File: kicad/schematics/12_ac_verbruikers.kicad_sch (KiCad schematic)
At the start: 6 parts

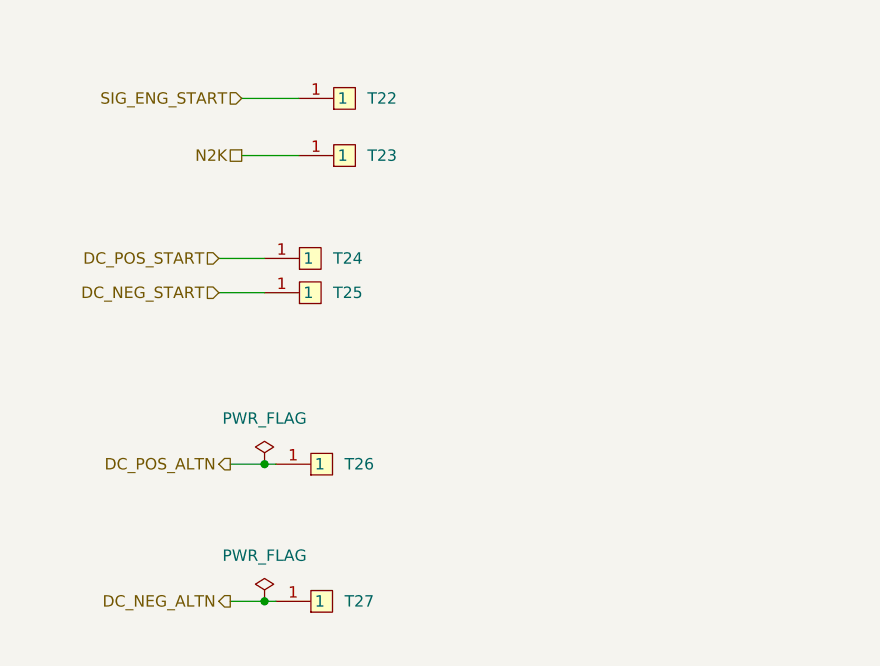
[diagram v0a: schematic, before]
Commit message: Introductie schema 15_energieconversie
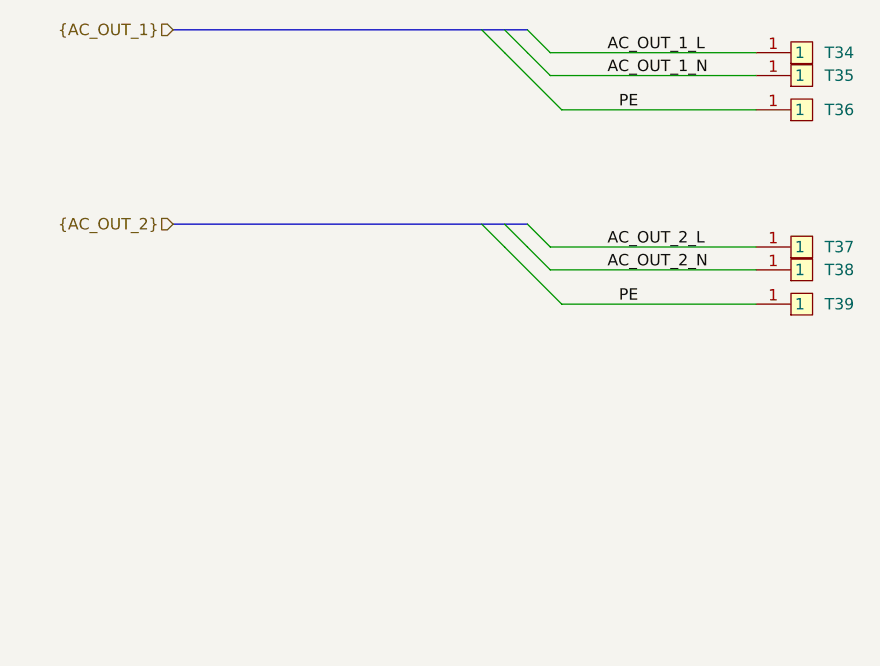
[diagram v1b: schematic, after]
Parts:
- removed T22, T23: (no value), symbol falkor-electrical:IF_Passief
- removed T24, T25, T26, T27: (no value), symbol falkor-electrical:IF_Power_Input
- added T34, T35, T37, T38: (no value), symbol falkor-electrical:IF_Power_Input
- added T36, T39: (no value), symbol falkor-electrical:IF_Passief
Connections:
- new net AC_OUT_1_L: T34.1
- new net AC_OUT_1_N: T35.1
- new net AC_OUT_2_L: T37.1
- new net AC_OUT_2_N: T38.1
- new net PE: T36.1, T39.1

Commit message: Schema's
00 toplevel stabiel
10 wisselstroom met subbladen stabiel
15 energieconversie stabiel
31 motor kern stabiel
32 motor sensoren stabiel
50 sensoren stabiel
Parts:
- renumbered T35 to T10, T36 to T11, T37 to T12, T38 to T13, T39 to T14, T34 to T9
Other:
- moved on the sheet: T10, T11, T12, T13, T14, T9
